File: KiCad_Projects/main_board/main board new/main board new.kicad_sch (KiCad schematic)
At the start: 76 parts

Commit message: 基板データの更新
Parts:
- removed C? (x3): C_Small, Capacitor_THT:C_Disc_D3.8mm_W2.6mm_P2.50mm, symbol Device:C_Small
- added C? (x3): C_Small, Capacitor_THT:C_Disc_D3.8mm_W2.6mm_P2.50mm, symbol Device:C_Small
- added D? (x3): WS2812B, LED_SMD:LED_WS2812B_PLCC4_5.0x5.0mm_P3.2mm, symbol LED:WS2812B
- added U?: Seeeduino_Xiao, Lib:seeeduinoXIAO, symbol seeeduino_xiao:Seeeduino_Xiao
- R? (x3): value 33k -> 22k
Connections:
- net +3V3: now also U?.12 (3V3)
- net +5V: now also U?.14 (5V)
- net AD3: now also C?.2
- net AD4: now also C?.2
- net AD5: now also C?.2
- net GND: now also C?.1, C?.1, C?.1, U?.13 (GND)
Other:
- moved on the sheet: C?, D?, J?, R?, SW?, U?

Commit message: 基板データの更新
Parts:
- removed D? (x2): WS2812B, LED_SMD:LED_WS2812B_PLCC4_5.0x5.0mm_P3.2mm, symbol LED:WS2812B
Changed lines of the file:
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@@
-    (pin "4")
-  )
-  (symbol (lib_id "LED:WS2812B") (at 241.3 76.2 0) (unit 1)
-    (in_bom yes) (on_board yes) (fields_autoplaced)
-    (property "Reference" "D?" (id 0) (at 252.73 71.8693 0))
-    (property "Value" "WS2812B" (id 1) (at 252.73 74.4093 0))
-    (property "Footprint" "LED_SMD:LED_WS2812B_PLCC4_5.0x5.0mm_P3.2mm" (id 2) (at 242.57 83.82 0)
-      (effects (font (size 1.27 1.27)) (justify left top) hide)
-    )
-    (property "Datasheet" "https://cdn-shop.adafruit.com/datasheets/WS2812B.pdf" (id 3) (at 243.84 85.725 0)
-      (effects (font (size 1.27 1.27)) (justify left top) hide)
-    )
-    (pin "1")
-    (pin "2")
-    (pin "3")
     (pin "4")
   )
@@
     (pin "2")
   )
-  (symbol (lib_id "LED:WS2812B") (at 208.28 69.85 0) (unit 1)
-    (in_bom yes) (on_board yes) (fields_autoplaced)
-    (property "Reference" "D?" (id 0) (at 219.71 65.5193 0))
-    (property "Value" "WS2812B" (id 1) (at 219.71 68.0593 0))
-    (property "Footprint" "LED_SMD:LED_WS2812B_PLCC4_5.0x5.0mm_P3.2mm" (id 2) (at 209.55 77.47 0)
-      (effects (font (size 1.27 1.27)) (justify left top) hide)
-    )
-    (property "Datasheet" "https://cdn-shop.adafruit.com/datasheets/WS2812B.pdf" (id 3) (at 210.82 79.375 0)
-      (effects (font (size 1.27 1.27)) (justify left top) hide)
-    )
-    (pin "1")
-    (pin "2")
-    (pin "3")
-    (pin "4")
-  )
   (symbol (lib_id "power:GND") (at 238.76 144.78 180) (unit 1)
     (in_bom yes) (on_board yes)
@@
       (reference "D?") (unit 1) (value "WS2812B") (footprint "LED_SMD:LED_WS2812B_PLCC4_5.0x5.0mm_P3.2mm")
     )
-    (path "/d6942b36-a4c5-49fe-b8f0-d27df7ea8e3e"
-      (reference "D?") (unit 1) (value "WS2812B") (footprint "LED_SMD:LED_WS2812B_PLCC4_5.0x5.0mm_P3.2mm")
-    )
-    (path "/dd8fb4c4-7542-4306-a8b0-0e4128575b37"
-      (reference "D?") (unit 1) (value "WS2812B") (footprint "LED_SMD:LED_WS2812B_PLCC4_5.0x5.0mm_P3.2mm")
-    )

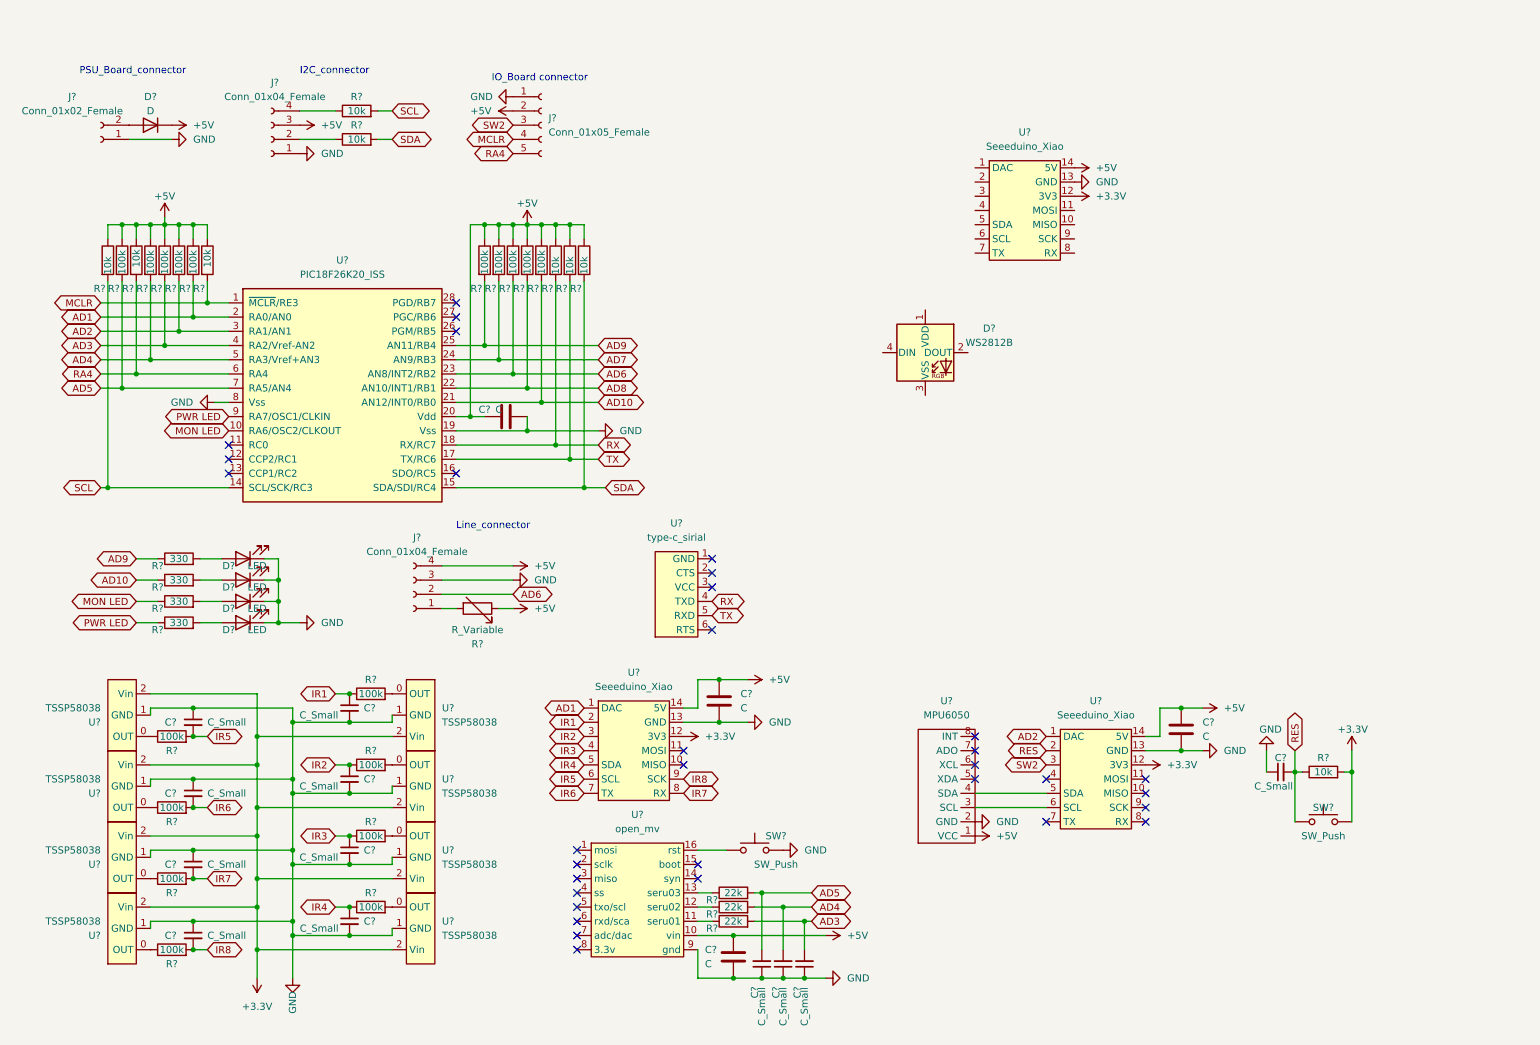
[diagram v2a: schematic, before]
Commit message: 基板データの更新
新メイン基板あたりをいじった
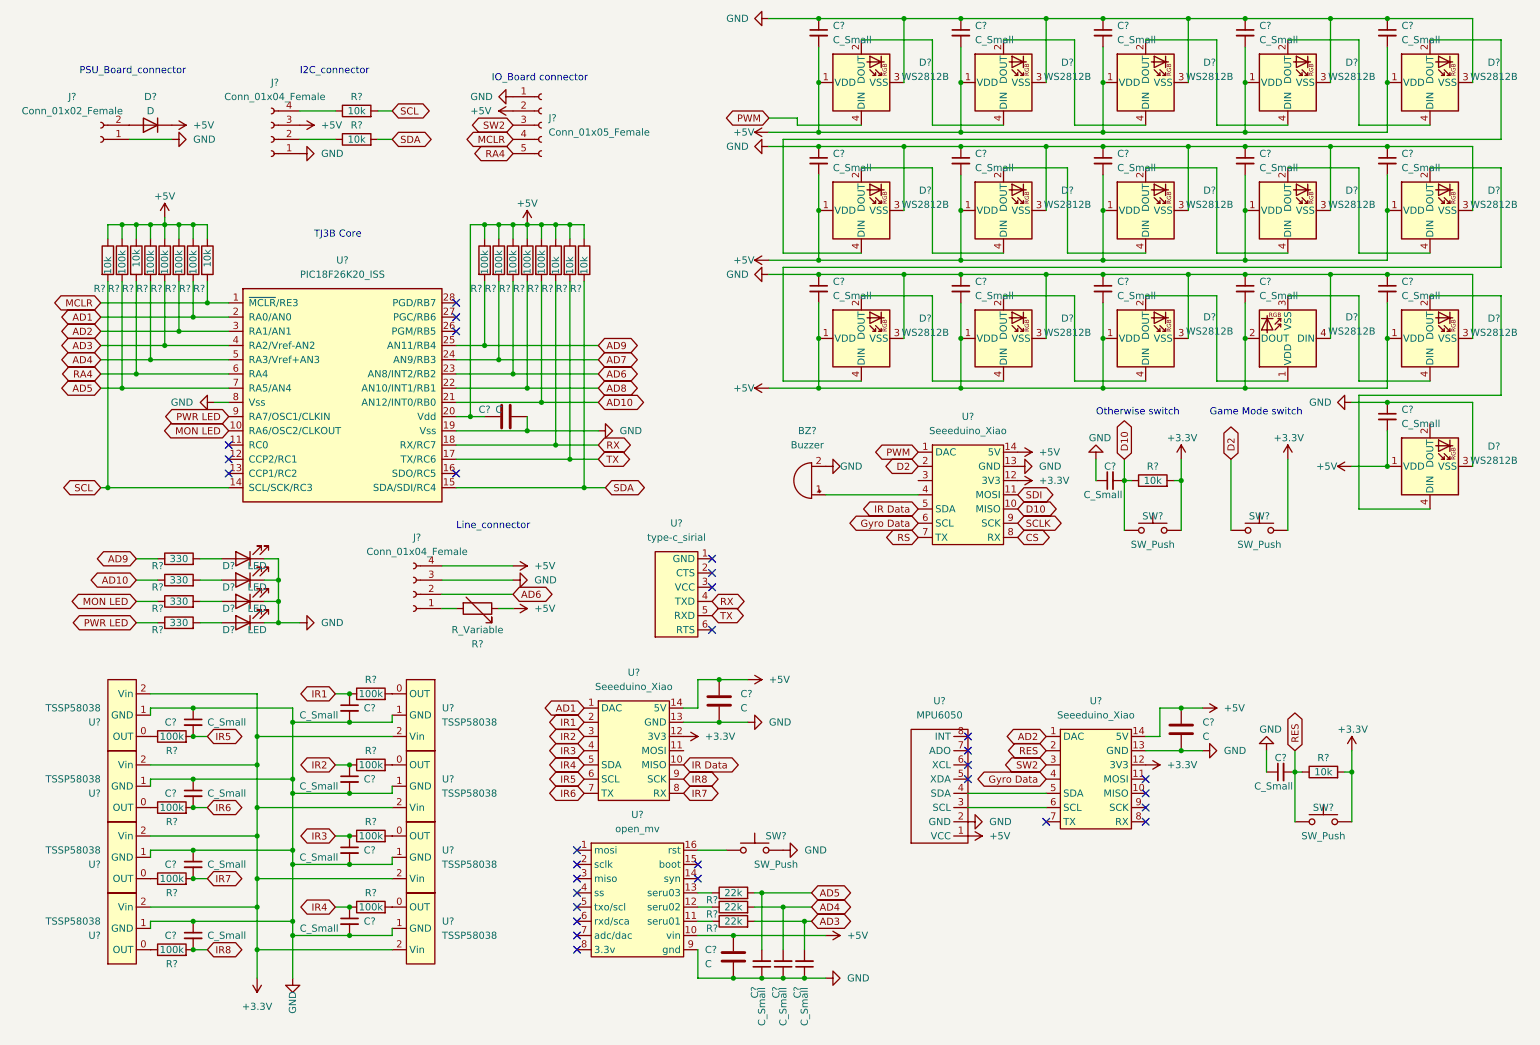
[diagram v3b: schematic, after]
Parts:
- added BZ?: Buzzer, symbol Device:Buzzer
- added C? (x16): C_Small, symbol Device:C_Small
- added C?: C_Small, Capacitor_THT:C_Disc_D3.8mm_W2.6mm_P2.50mm, symbol Device:C_Small
- added D? (x15): WS2812B, LED_SMD:LED_WS2812B_PLCC4_5.0x5.0mm_P3.2mm, symbol LED:WS2812B
- added R?: 10k, Resistor_THT:R_Axial_DIN0204_L3.6mm_D1.6mm_P5.08mm_Horizontal, symbol Device:R
- added SW? (x2): SW_Push, Button_Switch_THT:SW_PUSH_6mm_H5mm, symbol Switch:SW_Push
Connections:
- net +3V3: now also R?.2, SW?.2, SW?.2
- net +5V: now also D?.1 (VDD), C?.2, C?.2, C?.2, C?.2, C?.2, C?.2, C?.2, C?.2, C?.2, C?.2, C?.2, C?.2, C?.2, C?.2, C?.2, C?.2, D?.1 (VDD), D?.1 (VDD), D?.1 (VDD), D?.1 (VDD), D?.1 (VDD), D?.1 (VDD), D?.1 (VDD), D?.1 (VDD), D?.1 (VDD), D?.1 (VDD), D?.1 (VDD), D?.1 (VDD), D?.1 (VDD), D?.1 (VDD), D?.2 (DOUT)
- net GND: now also D?.3 (VSS), BZ?.2 (+), C?.1, C?.1, C?.1, C?.1, C?.1, C?.1, C?.1, C?.1, C?.1, C?.1, C?.1, C?.1, C?.1, C?.1, C?.1, C?.1, C?.1, D?.3 (VSS), D?.3 (VSS), D?.3 (VSS), D?.3 (VSS), D?.3 (VSS), D?.3 (VSS), D?.3 (VSS), D?.3 (VSS), D?.3 (VSS), D?.3 (VSS), D?.3 (VSS), D?.3 (VSS), D?.3 (VSS), D?.3 (VSS), D?.4 (DIN)
- net IR Data: now reaches U?.10 (MISO)
- net IR Data: now also U?.5 (SDA)
- net Gyro Data: now reaches U?.4
- net Gyro Data: now also U?.6 (SCL)
- net PWM: now reaches U?.1 (DAC)
- net PWM: now also D?.4 (DIN)
- net D10: now reaches U?.10 (MISO)
- net D10: now also C?.2, R?.1, SW?.1
- net SDI: now reaches U?.11 (MOSI)
- net D2: now reaches U?.2
- net D2: now also SW?.1
- net at U?.4: now also BZ?.1 (-)
- net RS: now reaches U?.7 (TX)
- net CS: now reaches U?.8 (RX)
- net SCLK: now reaches U?.9 (SCK)
- net at D?.2 (DOUT): now also D?.4 (DIN)
- new net: D?.2 (DOUT), D?.4 (DIN) (x12)
- new net: D?.1 (VDD), D?.2 (DOUT)
- new net: D?.3 (VSS), D?.4 (DIN)
- no-connect marks 33 -> 30
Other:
- note added: "Game Mode switch"
- note added: "Otherwise switch"
- note added: "TJ3B Core"
- moved on the sheet: D?, U?

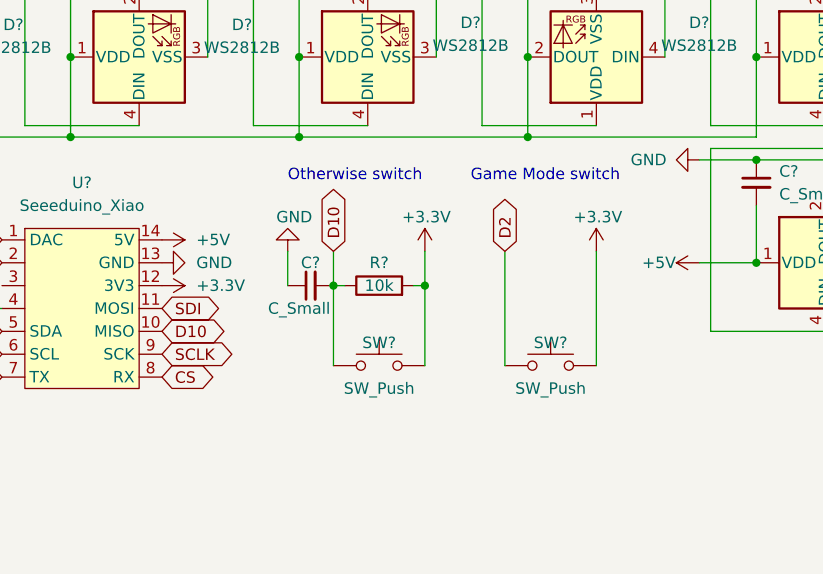
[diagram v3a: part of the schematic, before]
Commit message: 基板データの更新
いろいろいじったものの更新です。
MD用のファイルの追加もしました。
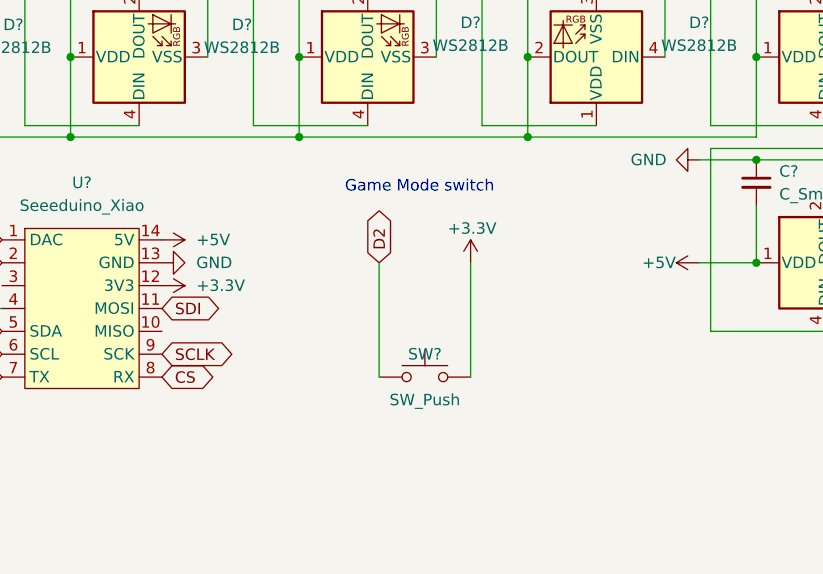
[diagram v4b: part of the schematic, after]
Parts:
- removed C?: C_Small, Capacitor_THT:C_Disc_D3.8mm_W2.6mm_P2.50mm, symbol Device:C_Small
- removed R?: 10k, Resistor_THT:R_Axial_DIN0204_L3.6mm_D1.6mm_P5.08mm_Horizontal, symbol Device:R
- removed SW?: SW_Push, Button_Switch_THT:SW_PUSH_6mm_H5mm, symbol Switch:SW_Push
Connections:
- net D10: no longer names the net of U?.10 (MISO)
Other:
- note removed: "Otherwise switch"
- moved on the sheet: SW?

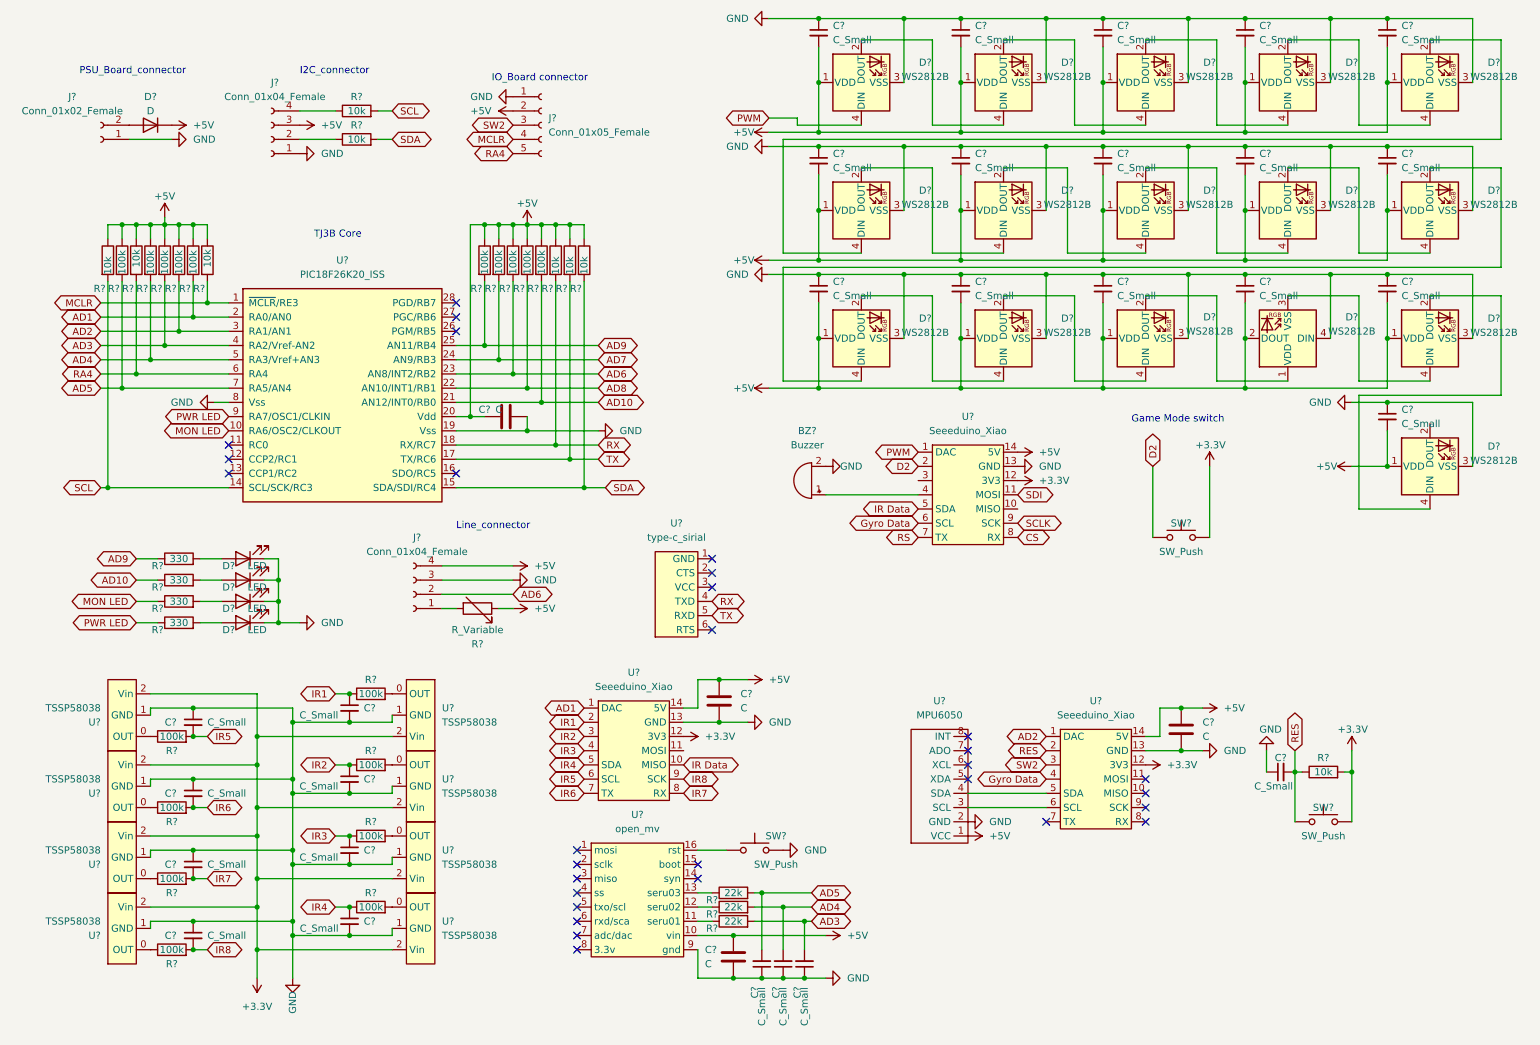
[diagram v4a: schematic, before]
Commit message: 基板データの更新
新メイン基板のデータの更新
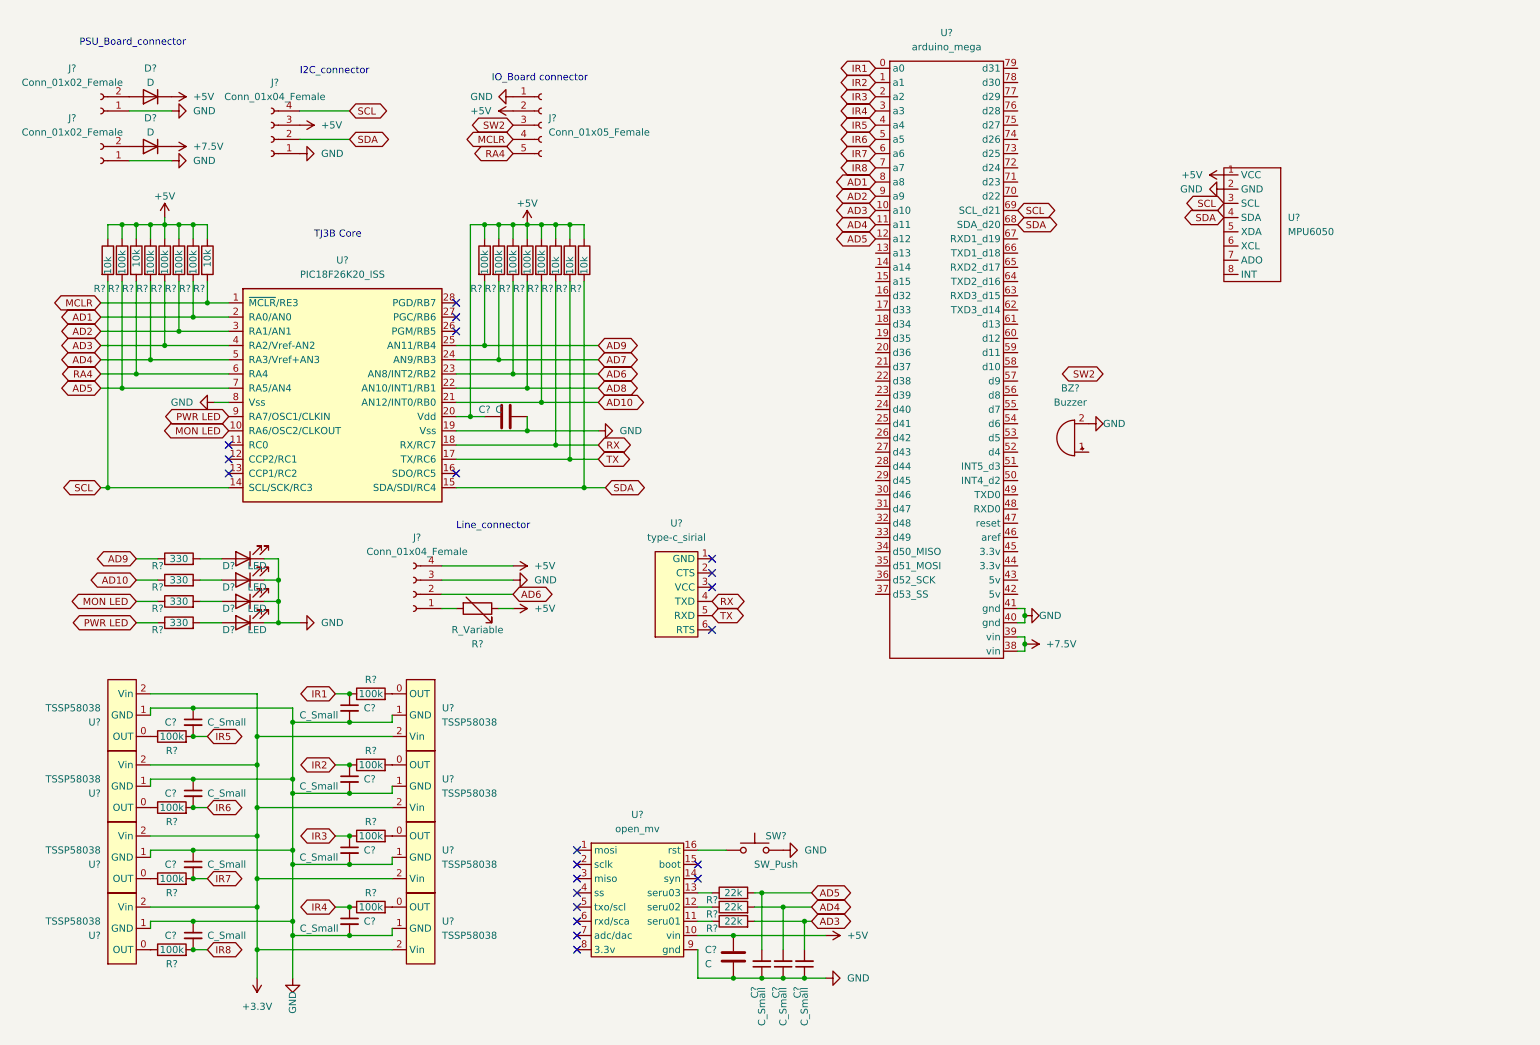
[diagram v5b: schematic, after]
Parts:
- removed BZ?: Buzzer, symbol Device:Buzzer
- removed C? (x16): C_Small, symbol Device:C_Small
- removed C? (x2): C, Capacitor_THT:CP_Radial_D5.0mm_P2.50mm, symbol Device:C
- removed C?: C_Small, Capacitor_THT:C_Disc_D3.8mm_W2.6mm_P2.50mm, symbol Device:C_Small
- removed D? (x16): WS2812B, LED_SMD:LED_WS2812B_PLCC4_5.0x5.0mm_P3.2mm, symbol LED:WS2812B
- removed R? (x3): 10k, Resistor_THT:R_Axial_DIN0204_L3.6mm_D1.6mm_P5.08mm_Horizontal, symbol Device:R
- removed SW? (x2): SW_Push, Button_Switch_THT:SW_PUSH_6mm_H5mm, symbol Switch:SW_Push
- removed U? (x3): Seeeduino_Xiao, Lib:seeeduinoXIAO, symbol seeeduino_xiao:Seeeduino_Xiao
- removed U?: MPU6050, Lib:MPU6050, symbol mpu6050:MPU6050
- added BZ?: Buzzer, symbol Device:Buzzer
- added D?: D, Diode_THT:D_DO-41_SOD81_P7.62mm_Horizontal, symbol Device:D
- added J?: Conn_01x02_Female, Connector_JST:JST_XH_B2B-XH-A_1x02_P2.50mm_Vertical, symbol Connector:Conn_01x02_Female
- added U?: arduino_mega, symbol arduino mega:arduino_mega
- added U?: MPU6050, Lib:MPU6050, symbol mpu6050:MPU6050
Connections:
- net +5V: now also U?.1 (VCC)
- net AD1: now also U?.8 (a8)
- net AD2: now also U?.9 (a9)
- net AD3: now also U?.10 (a10)
- net AD4: now also U?.11 (a11)
- net AD5: now also U?.12 (a12)
- net GND: now also BZ?.2 (+), J?.1 (Pin_1), U?.2 (GND), U?.40 (gnd), U?.41 (gnd)
- net IR1: now also U?.0 (a0)
- net IR2: now also U?.1 (a1)
- net IR3: now also U?.2 (a2)
- net IR4: now also U?.3 (a3)
- net IR5: now also U?.4 (a4)
- net IR6: now also U?.5 (a5)
- net IR7: now also U?.6 (a6)
- net IR8: now also U?.7 (a7)
- net SCL: now also J?.4 (Pin_4), U?.3 (SCL), U?.69 (SCL_d21)
- net SDA: now also J?.2 (Pin_2), U?.4 (SDA), U?.68 (SDA_d20)
- new net: D?.2 (A), J?.2 (Pin_2)
- new net +7.5V: D?.1 (K), U?.38 (vin), U?.39 (vin)
- no-connect marks 30 -> 21
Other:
- note removed: "Game Mode switch"
- moved on the sheet: D?, J?
